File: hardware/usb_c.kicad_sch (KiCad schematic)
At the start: 16 parts, among them IC5 TCPP01-M12, J3 UJC-H-G-SMT-2-P6-TR, Q5 STL11N3LLH6

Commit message: Battery temperature meter added to MCU
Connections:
- net 3V3 renamed +3V3
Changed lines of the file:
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@@
 	(wire
 		(pts
-			(xy 233.68 143.51) (xy 204.47 143.51)
+			(xy 204.47 143.51) (xy 247.65 143.51)
 		)
 		(stroke
@@
 		(pts
 			(xy 166.37 101.6) (xy 166.37 125.73)
+		)
+		(stroke
+			(width 0)
+			(type default)
+		)
+	)
+	(wire
+		(pts
+			(xy 247.65 142.24) (xy 247.65 143.51)
 		)
 		(stroke
@@
 		(exclude_from_sim no)
 		(at 200.406 119.38 0)
-		(effects
-			(font
-				(size 1.27 1.27)
-			)
-			(justify left)
-		)
-	)
-	(hierarchical_label "3V3"
-		(shape input)
-		(at 233.68 143.51 0)
 		(effects
 			(font
@@
 					(unit 1)
 				)
+			)
+		)
+	)
+	(symbol
+		(lib_id "power:+3V3")
+		(at 247.65 142.24 0)
+		(unit 1)
+		(exclude_from_sim no)
+		(in_bom yes)
+		(on_board yes)
+		(dnp no)
+		(property "Reference" "#PWR068"
+			(at 247.65 146.05 0)
+			(effects
+				(font
+					(size 1.27 1.27)
+				)
+				(hide yes)
+			)
+		)
+		(property "Value" "+3V3"
+			(at 246.888 138.176 0)
+			(effects
+				(font
+					(size 1.27 1.27)
+				)
+			)
+		)
+		(property "Footprint" ""
+			(at 247.65 142.24 0)
+			(effects
+				(font
+					(size 1.27 1.27)
+				)
+				(hide yes)
+			)
+		)
+		(property "Datasheet" ""
+			(at 247.65 142.24 0)
+			(effects
+				(font
+					(size 1.27 1.27)
+				)
+				(hide yes)
+			)
+		)
+		(property "Description" "Power symbol creates a global label with name \"+3V3\""
+			(at 247.65 142.24 0)
+			(effects
+				(font
+					(size 1.27 1.27)
+				)
+				(hide yes)
+			)
+		)
+		(pin "1"
+		)
+		(instances
+			(project "obvod"
+				(path "/e8e834c4-1afb-42f7-b718-3cb720dae1d5/540adf6e-5b6f-4df1-af18-d763618ddc56"
+					(reference "#PWR068")
+					(unit 1)
+				)

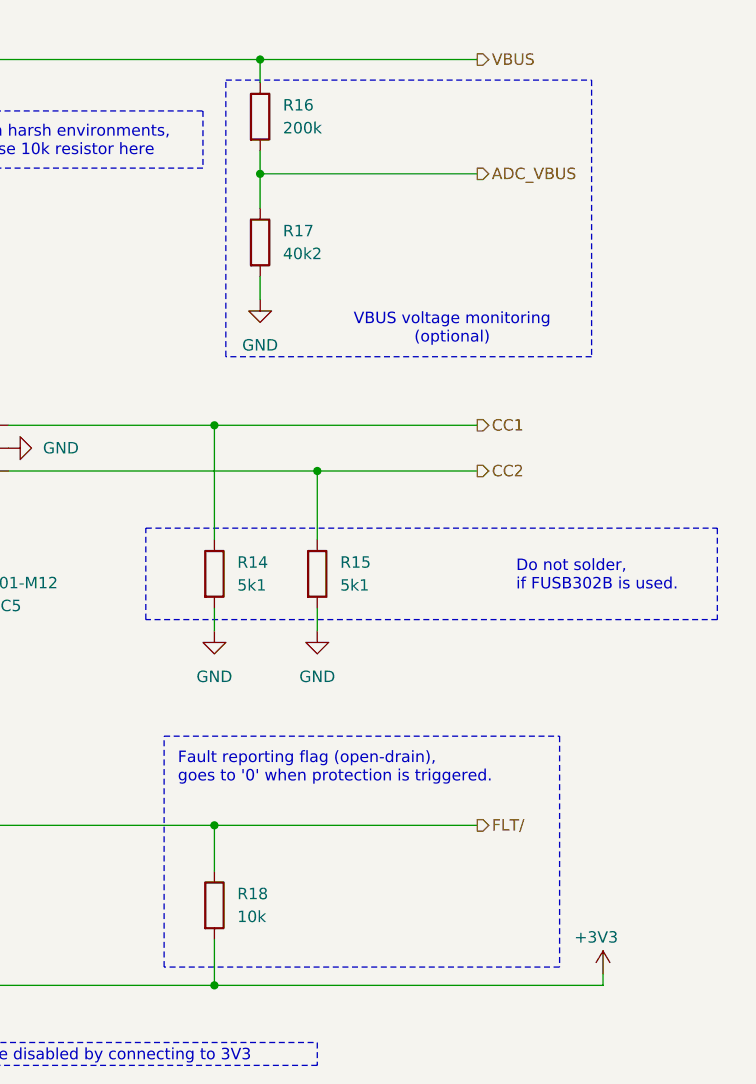
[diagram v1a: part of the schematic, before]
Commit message: Board connector added
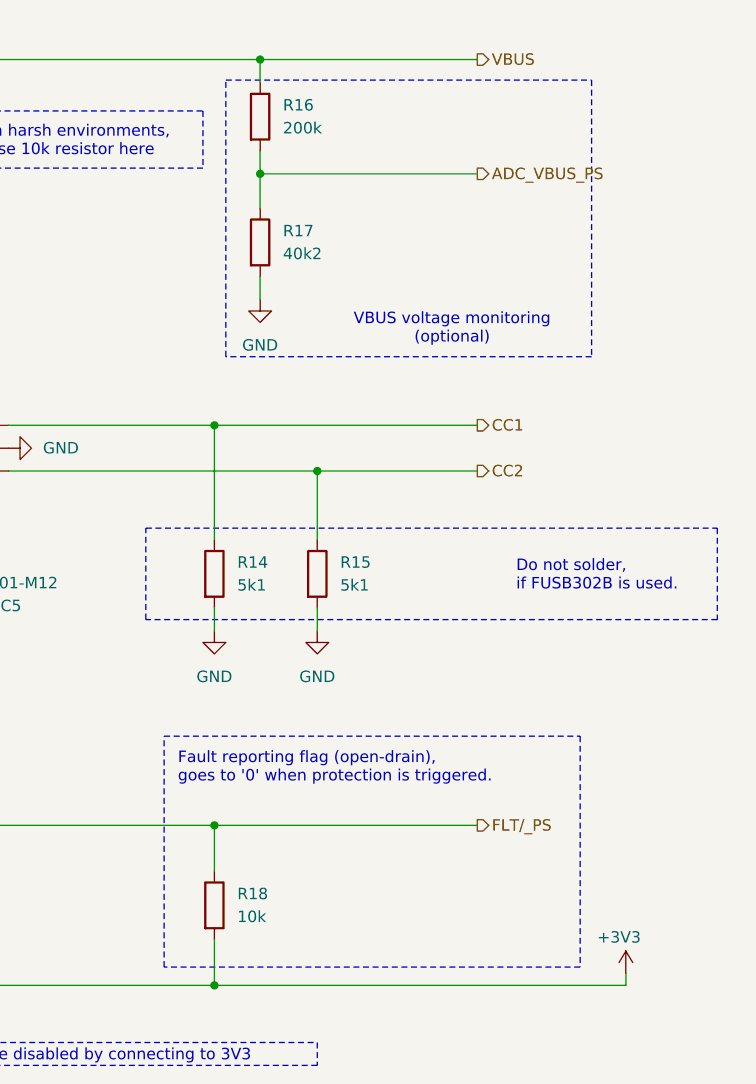
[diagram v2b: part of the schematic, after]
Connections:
- net ADC_VBUS renamed ADC_VBUS_PS
- net FLT/ renamed FLT/_PS
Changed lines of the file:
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@@
 	(wire
 		(pts
-			(xy 204.47 143.51) (xy 247.65 143.51)
+			(xy 204.47 143.51) (xy 250.19 143.51)
 		)
 		(stroke
@@
 	(wire
 		(pts
-			(xy 247.65 142.24) (xy 247.65 143.51)
+			(xy 250.19 142.24) (xy 250.19 143.51)
 		)
 		(stroke
@@
 	(rectangle
 		(start 198.882 115.824)
-		(end 242.824 141.478)
+		(end 245.11 141.478)
 		(stroke
 			(width 0)
@@
 		)
 	)
-	(hierarchical_label "ADC_VBUS"
+	(hierarchical_label "ADC_VBUS_PS"
 		(shape output)
 		(at 233.68 53.34 0)
@@
 		)
 	)
-	(hierarchical_label "FLT{slash}"
+	(hierarchical_label "FLT{slash}_PS"
 		(shape output)
 		(at 233.68 125.73 0)
@@
 	(symbol
 		(lib_id "power:+3V3")
-		(at 247.65 142.24 0)
+		(at 250.19 142.24 0)
 		(unit 1)
 		(exclude_from_sim no)
@@
 		(dnp no)
 		(property "Reference" "#PWR068"
-			(at 247.65 146.05 0)
+			(at 250.19 146.05 0)
 			(effects
 				(font
@@
 		)
 		(property "Value" "+3V3"
-			(at 246.888 138.176 0)
+			(at 249.428 138.176 0)
 			(effects
 				(font
@@
 		)
 		(property "Footprint" ""
-			(at 247.65 142.24 0)
+			(at 250.19 142.24 0)
 			(effects
 				(font
@@
 		)
 		(property "Datasheet" ""
-			(at 247.65 142.24 0)
+			(at 250.19 142.24 0)
 			(effects
 				(font
@@
 		)
 		(property "Description" "Power symbol creates a global label with name \"+3V3\""
-			(at 247.65 142.24 0)
-			(effects
-				(font
+			(at 250.19 142.24 0)
+			(effects
+				(font

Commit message: Revised and completed BOM
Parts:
- removed R16: 200k, Resistor_SMD:R_0603_1608Metric, symbol Device:R
- removed R17: 40k2, Resistor_SMD:R_0603_1608Metric, symbol Device:R
- added R13: 1k69, Resistor_SMD:R_0402_1005Metric, symbol Device:R
- added R14: 3k3, Resistor_SMD:R_0402_1005Metric, symbol Device:R
- R10: footprint Resistor_SMD:R_0603_1608Metric -> Resistor_SMD:R_0402_1005Metric
- R11: renamed from R12; footprint Resistor_SMD:R_0603_1608Metric -> Resistor_SMD:R_0402_1005Metric
- R17: renamed from R18; footprint Resistor_SMD:R_0603_1608Metric -> Resistor_SMD:R_0402_1005Metric
- renumbered C24 to C10, C23 to C8, C22 to C9, D4 to D3, D5 to D4, J3 to J1, Q5 to Q4, R13 to R12, R14 to R15, R15 to R16
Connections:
- net ADC_VBUS_PS: now also R13.2, R14.1
- net GND: now also R14.2
- net VBUS: now also R13.1
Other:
- note added: "VBUS voltage monitoring (not required)"
- note removed: "VBUS voltage monitoring (optional)"
- moved on the sheet: R12
